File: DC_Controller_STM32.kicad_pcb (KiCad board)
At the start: 4 copper layers, 154 x 154 mm, 293 parts, among them J1 SM08B-CPTK-1A-TBL, J10 Conn_01x04, J11 Conn_02x06_Odd_Even, J12 Conn_01x03, J13 Conn_01x02, J14 Conn_02x05_Odd_Even, J15 Conn_01x06, J16 TC2030-MCP, J17 Conn_01x04, J18 TC2030-MCP, J19 Conn_01x02, J2 Conn_02x20_Odd_Even, J3 SM02B-CPTK-1A-TB, J4 Conn_01x04, J5 BM02B-CPTK-1A-TB, J6 BM50B-SHLDS-G-TFT, J7 SM08B-CPTK-1A-TB, J8 BM08B-CPTK-1A-TB, J9 Conn_02x05_Odd_Even, Q1 NCV8402A, Q10 MMBT3904, Q11 MMBT3904, Q12 MMBT3904, Q13 MMBT3904, Q14 MMBT3904, Q15 MMBT3904, Q16 MMBT3904, Q17 MMBT3904, Q18 MMBT3904, Q19 MMBT3904, Q2 MMBT3904, Q20 MMBT3904, Q21 MMBT3904, Q22 MMBT3904, Q23 MMBT3904, Q24 MMBT3904, Q25 MMBT3904, Q3 S8050, Q4 S8050, Q5 NCV8402A, Q6 NCV8402A, Q7 NCV8402A, Q8 NCV8402A, Q9 NCV8402A, SW1 SW_Push, U1 MCP6561x-LT, U10 LM2776, U11 MP2359, U12 XC6206P332MR, U13 MC34063ABD-TR, U15 MAX889RESA+, U2 74LVC1G3157GW, U3 STM32F103RBT6, U4 SN65HVD230, U5 74LVC1G3157GW, U6 MCP2515-I/SO, U7 LTC6992CS6-1, U8 TJA1050T, U9 ATmega328P-AU, Y1 16MHz, Y2 8M0, Y3 16MHz

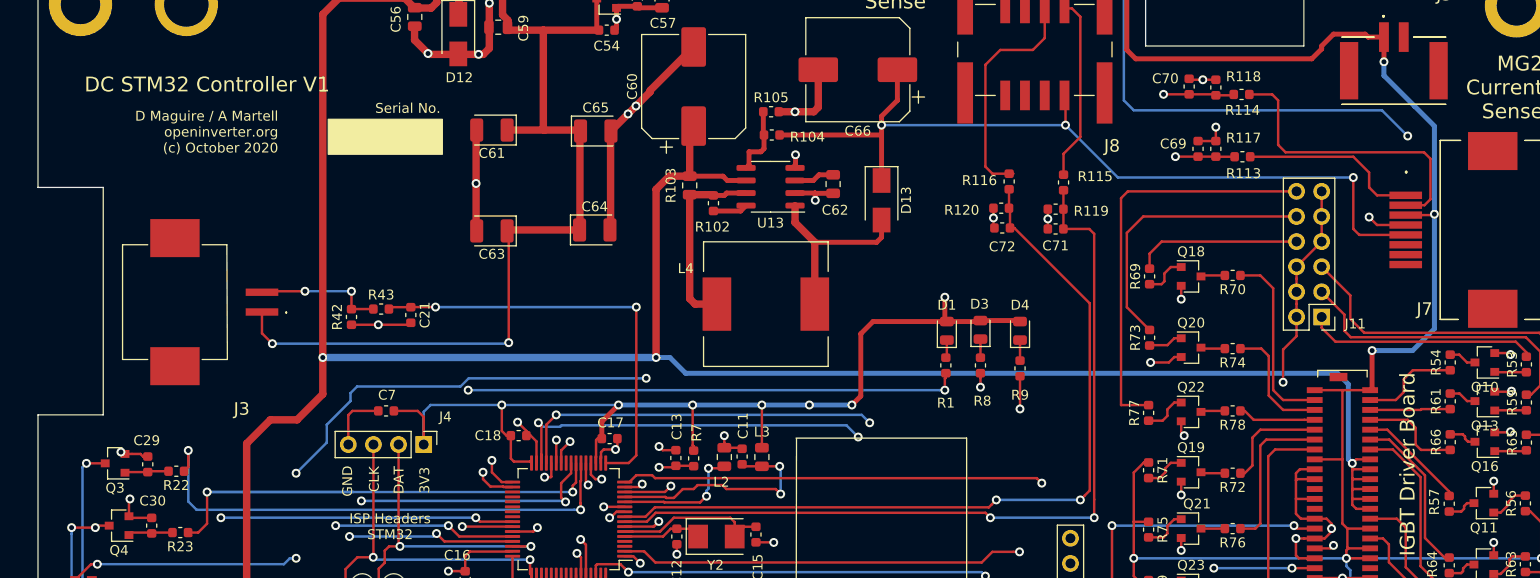
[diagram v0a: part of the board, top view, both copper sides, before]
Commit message: corrected tracking error around MG1 and MG current sensors.  J7 footprint updated (J1 left unchanged as tracking layout is currently ok).
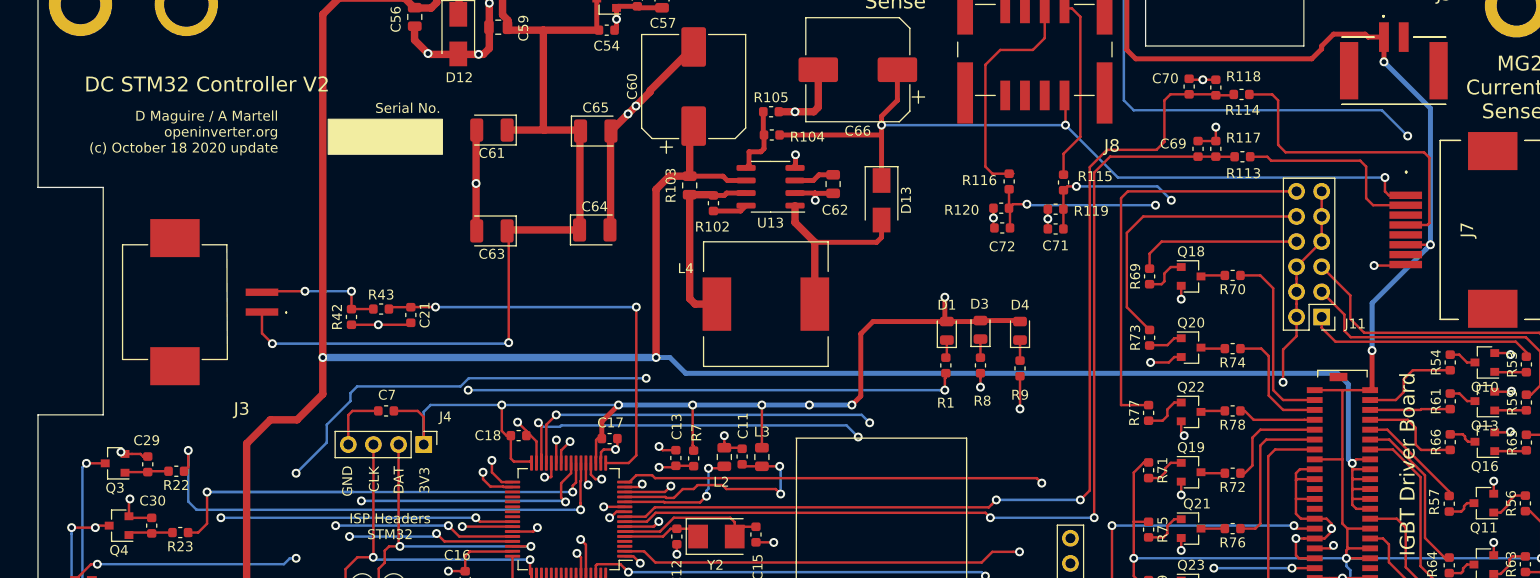
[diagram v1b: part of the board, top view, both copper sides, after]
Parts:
- J7: footprint SamacSys_Parts:SM08BCPTK1ATBL -> SamacSys_Parts:SM08BCPTK1ATBL_odd_even
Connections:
- C69 pad 1: MG1_I1 -> PC0_MG2_IL1
- C70 pad 1: MG1_I2 -> PC1_MG2_IL2
- C71 pad 1: PC0_MG2_IL1 -> MG1_I1
- C72 pad 1: PC1_MG2_IL2 -> MG1_I2
- J7 pad 1: MG1_IL1_In -> MG2_IL1_In
- J7 pad 2: MG1_IL2_In -> MG2_IL2_In
- J8 pad 1: MG2_IL1_In -> MG1_IL1_In
- J8 pad 2: MG2_IL2_In -> MG1_IL2_In
- R113 pad 1: MG1_IL1_In -> MG2_IL1_In
- R113 pad 2: MG1_I1 -> PC0_MG2_IL1
- R114 pad 1: MG1_IL2_In -> MG2_IL2_In
- R114 pad 2: MG1_I2 -> PC1_MG2_IL2
- R115 pad 1: MG2_IL1_In -> MG1_IL1_In
- R115 pad 2: PC0_MG2_IL1 -> MG1_I1
- R116 pad 1: MG2_IL2_In -> MG1_IL2_In
- R116 pad 2: PC1_MG2_IL2 -> MG1_I2
- R117 pad 2: MG1_I1 -> PC0_MG2_IL1
- R118 pad 2: MG1_I2 -> PC1_MG2_IL2
- R119 pad 2: PC0_MG2_IL1 -> MG1_I1
- R120 pad 2: PC1_MG2_IL2 -> MG1_I2
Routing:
- net PC1_MG2_IL2: track 82.2 -> 101.0 mm
- net PC0_MG2_IL1: track 84.0 -> 97.8 mm
- net MG2_IL2_In: track 23.9 -> 32.6 mm
- net MG1_IL2_In: track 30.5 -> 23.9 mm
- net MG1_I1: track 152.5 -> 157.4 mm, vias 3 -> 4
- net Vcc_26V: track 85.9 -> 82.0 mm
- net +5V: track 818.7 -> 815.5 mm
- net -5V: track 172.1 -> 170.5 mm
- net MG2_IL1_In: track 18.6 -> 19.6 mm
- net MG1_I2: track 155.9 -> 156.8 mm, vias 3 -> 4
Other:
- board text added: "D Maguire / A Martell openinverter.org (c) October 18 2020 update"
- board text added: "DC STM32 Controller V2"
- board text removed: "D Maguire / A Martell openinverter.org (c) October 2020"
- board text removed: "DC STM32 Controller V1"
